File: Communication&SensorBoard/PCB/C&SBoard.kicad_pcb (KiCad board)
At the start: 2 copper layers, 93.3 x 93.3 mm, 74 parts, among them J1 NebulaConnector, J10 Conn_01x02, J11 Conn_Coaxial, J2 Conn_Coaxial, J3 Conn_01x04, J4 Conn_02x09_Odd_Even, J5 Micro_SD_Card, J6 Conn_01x03, J7 Conn_01x02, J8 Conn_01x02, J9 Conn_01x02, Q1 NPN, Q2 NPN, Q3 NMOS, Q4 NMOS, Q5 NPN, Q6 NPN, Q7 NMOS, Q8 NMOS, SW1 SW_Push, SW2 SW_SPDT, U1 E22-400M22S, U2 ESP32-S3-MINI-1U, U3 ST LIV3R, U4 TPS294x, U5 BMI270, U6 BMP390, U7 HDC1080, U8 LIS2MDL

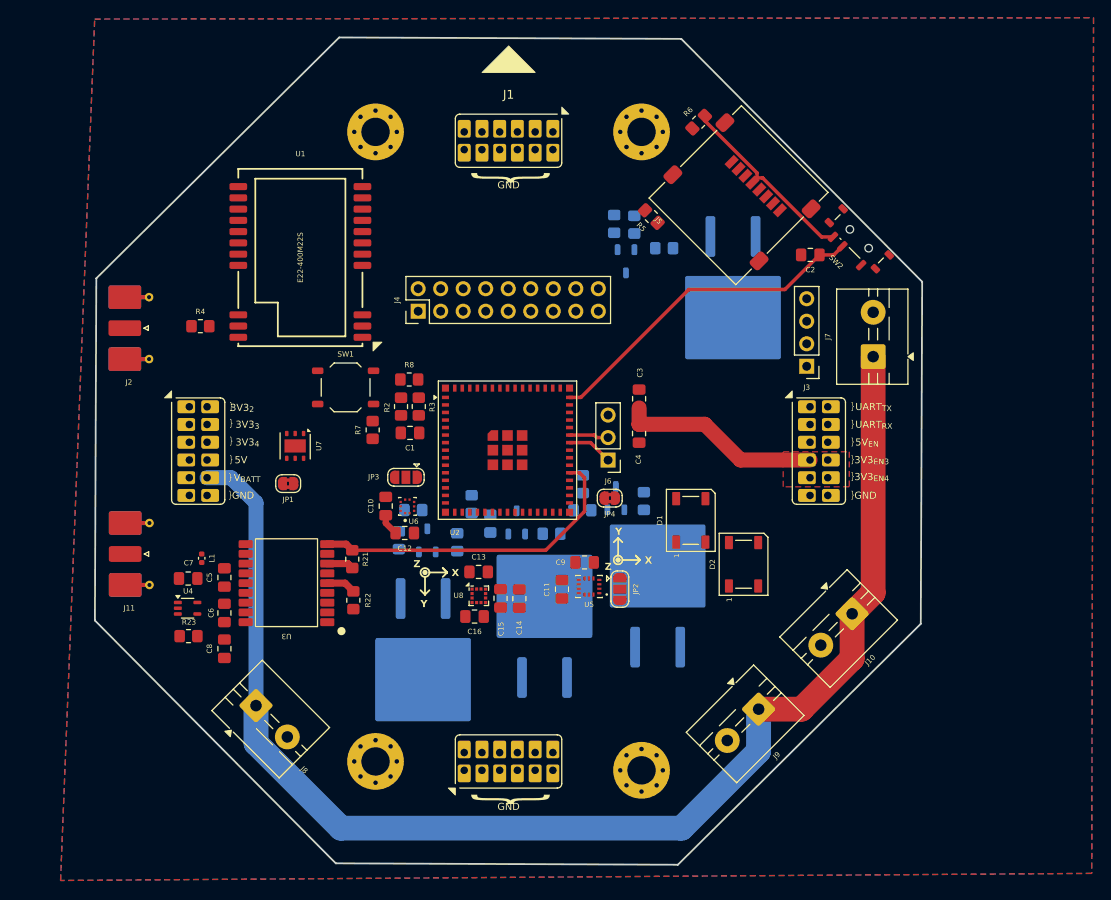
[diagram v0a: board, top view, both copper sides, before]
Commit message: C&S board - update GPS
se cambio el conector del gps pasando de un sistema incorporado en placa a un sistema externo, con el BZ251
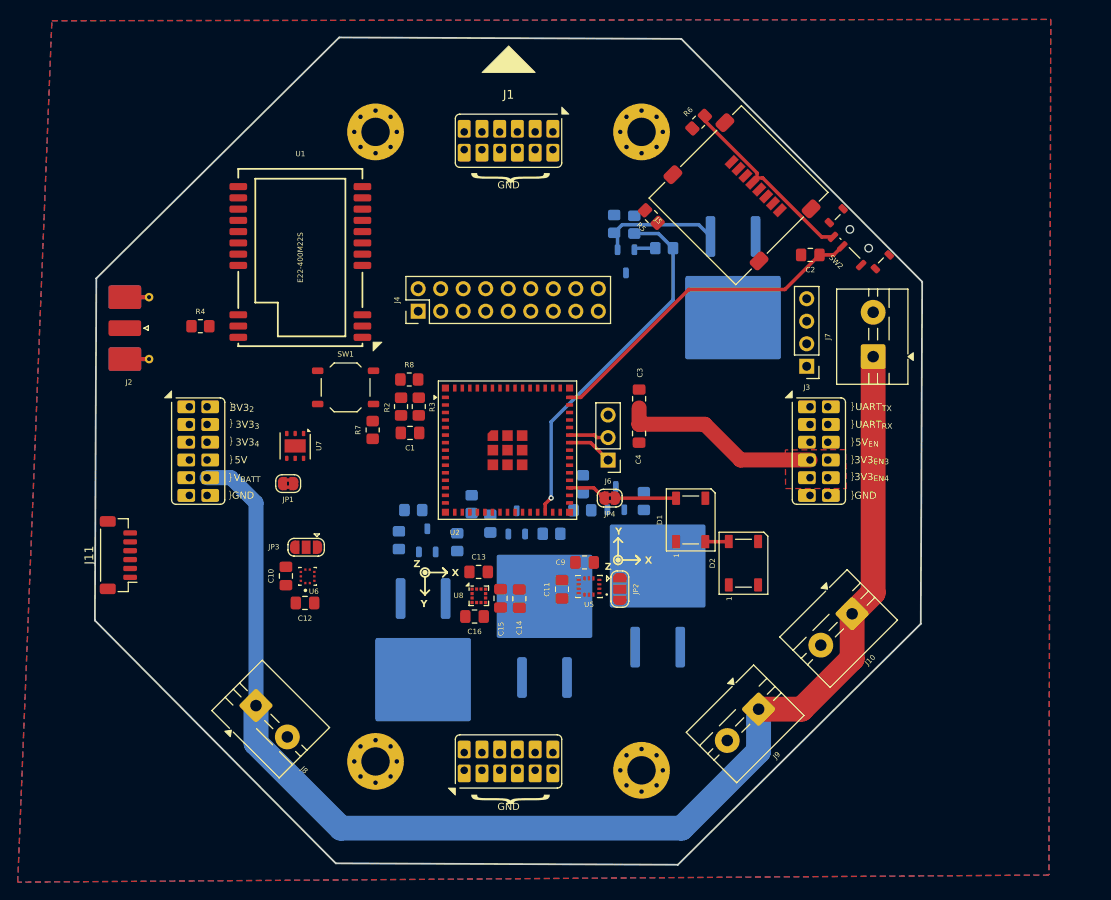
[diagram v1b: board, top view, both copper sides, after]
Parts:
- removed C5: 56pf, Capacitor_SMD:C_0805_2012Metric_Pad1.18x1.45mm_HandSolder
- removed C6, C7: 56pF, Capacitor_SMD:C_0805_2012Metric_Pad1.18x1.45mm_HandSolder
- removed C8: 10uF, Capacitor_SMD:C_0805_2012Metric_Pad1.18x1.45mm_HandSolder
- removed L1: 5.6nH, Capacitor_SMD:C_0402_1005Metric
- removed R21, R22: 10k, Resistor_SMD:R_0805_2012Metric_Pad1.20x1.40mm_HandSolder
- removed R23: 100k, Resistor_SMD:R_0805_2012Metric_Pad1.20x1.40mm_HandSolder
- removed U3: ST LIV3R, CompVuelo:LIV3F
- removed U4: TPS294x, Package_TO_SOT_SMD:Texas_R-PDSO-G5_DCK-5
- J11: value Conn_Coaxial -> Conn_01x06; footprint Connector_Coaxial:SMA_Molex_73251-2120_EdgeMount_Horizontal -> Connector_JST:JST_SH_BM06B-SRSS-TB_1x06-1MP_P1.00mm_Vertical
- moved JP3 13.7 mm to (66.3, 94.6)
- moved C10 13.7 mm to (64.0, 97.9)
- moved C12 13.7 mm to (66.2, 100.9)
- moved U6 13.7 mm to (66.5, 97.9)
- moved J11 0.53 mm to (45.1, 95.5), turned to 90 degrees
- moved D2 0.12 mm to (115.6, 96.4)
- moved D1 0.05 mm to (109.7, 91.5)
- turned R11 to 180 degrees
- turned R13 to -90 degrees
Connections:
- J11 pad 1: Net-(J11-In) -> /UART_{TX}
- J11 pad 2: GND -> /UART_{RX}
- U2 pad 34: /WK_{up} -> unconnected-(U2-IO38-Pad34)
- U2 pad 35: /RST -> unconnected-(U2-IO39-Pad35)
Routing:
- net OUT_{1}: track 0.00 -> 40.8 mm, vias 0 -> 1
- net /RST: track 36.8 -> 0.00 mm
- net Net-(Q1-C): track 0.00 -> 13.9 mm
- net Net-(D1-DIN): track 0.00 -> 6.83 mm
- net DIN: track 0.00 -> 4.36 mm
- net /WK_{up}: track 3.33 -> 0.00 mm
- net 3V3_{2}: track 3.02 -> 0.00 mm
- net Net-(D1-DOUT): track 0.00 -> 2.70 mm
- net VDD: track 46.8 -> 44.3 mm
- net Net-(Q1-B): track 0.00 -> 2.43 mm

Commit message: C&S-board
se avanzo en el trazado de pistas
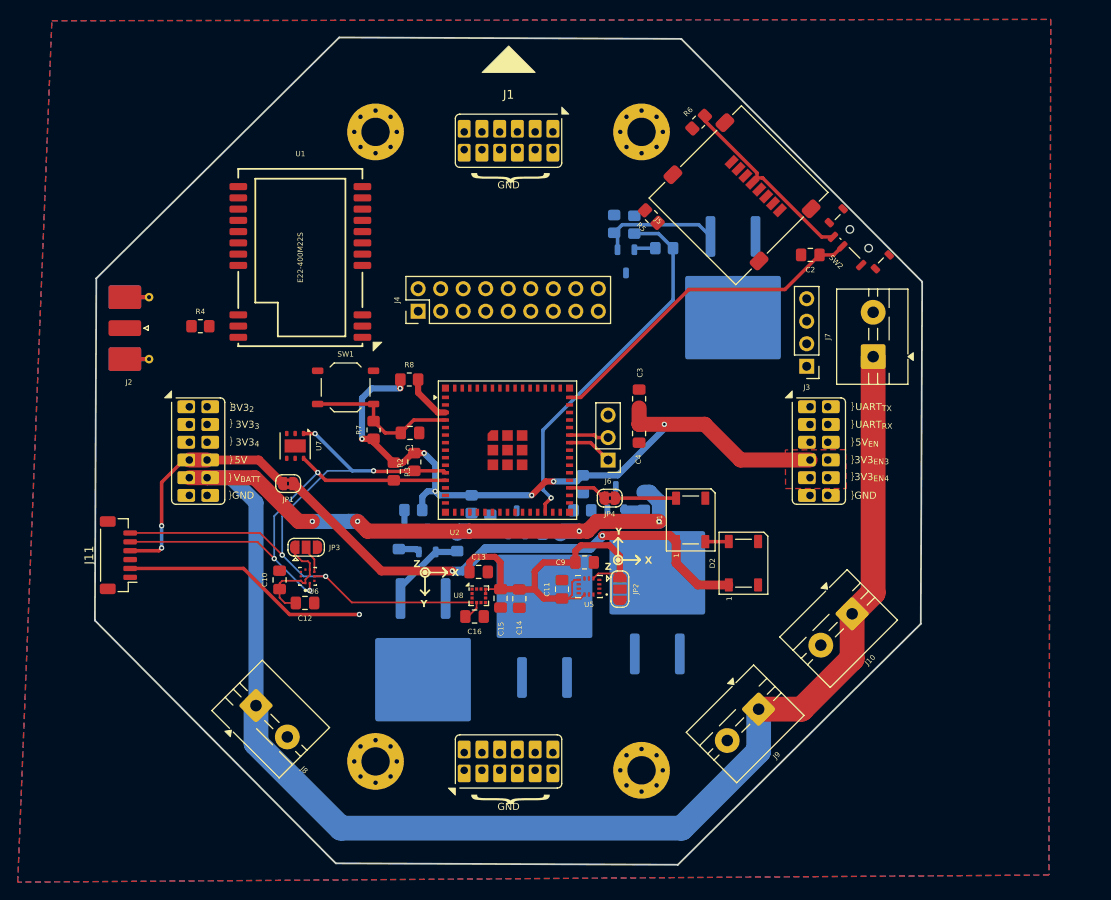
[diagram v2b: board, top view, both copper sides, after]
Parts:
- moved R3 7.84 mm to (76.2, 86.1)
- moved R2 6.43 mm to (78.5, 85.0)
- moved C10 0.84 mm to (63.3, 98.3)
- moved Q8 0.77 mm to (105.9, 99.0)
- moved R7 0.10 mm to (73.9, 81.4)
- turned JP3 to 0 degrees
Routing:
- net VDD: track 44.3 -> 157.3 mm, vias 0 -> 7
- net /SDA: track 0.00 -> 76.5 mm, vias 0 -> 4
- net +BATT: track 150.8 -> 215.0 mm, vias 0 -> 5
- net Net-(D1-VDD): track 0.00 -> 58.6 mm, vias 0 -> 2
- net /SCL: track 0.00 -> 52.1 mm, vias 0 -> 3
- net /UART_{RX}: track 0.00 -> 28.0 mm, vias 0 -> 1
- net +5V: track 0.00 -> 27.2 mm, vias 0 -> 2
- net /ESP32/ESP32_{EN}: track 0.00 -> 17.5 mm
- net Net-(Q2-C): track 0.00 -> 9.36 mm
- net Net-(U2-3V3): track 0.00 -> 5.50 mm
- net Net-(JP3-C): track 0.00 -> 3.16 mm
- net OUT_{2}: track 0.00 -> 2.66 mm
- net Net-(Q2-B): track 0.00 -> 2.38 mm
- net Net-(U8-C1): track 0.00 -> 2.29 mm
- net Net-(Q6-C): track 0.00 -> 2.23 mm
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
